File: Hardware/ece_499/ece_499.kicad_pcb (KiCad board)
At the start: 2 copper layers, 100 x 70 mm, 44 parts, among them J1 Conn_01x04, J2 Conn_01x04, J3 Conn_01x04, J4 Conn_01x04, J5 Conn_01x04, Q1 DMN2004WK, Q2 DMN2004WK, Q3 DMN2004WK, Q4 DMN2004WK, SW1 RotaryEncoder_Switch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

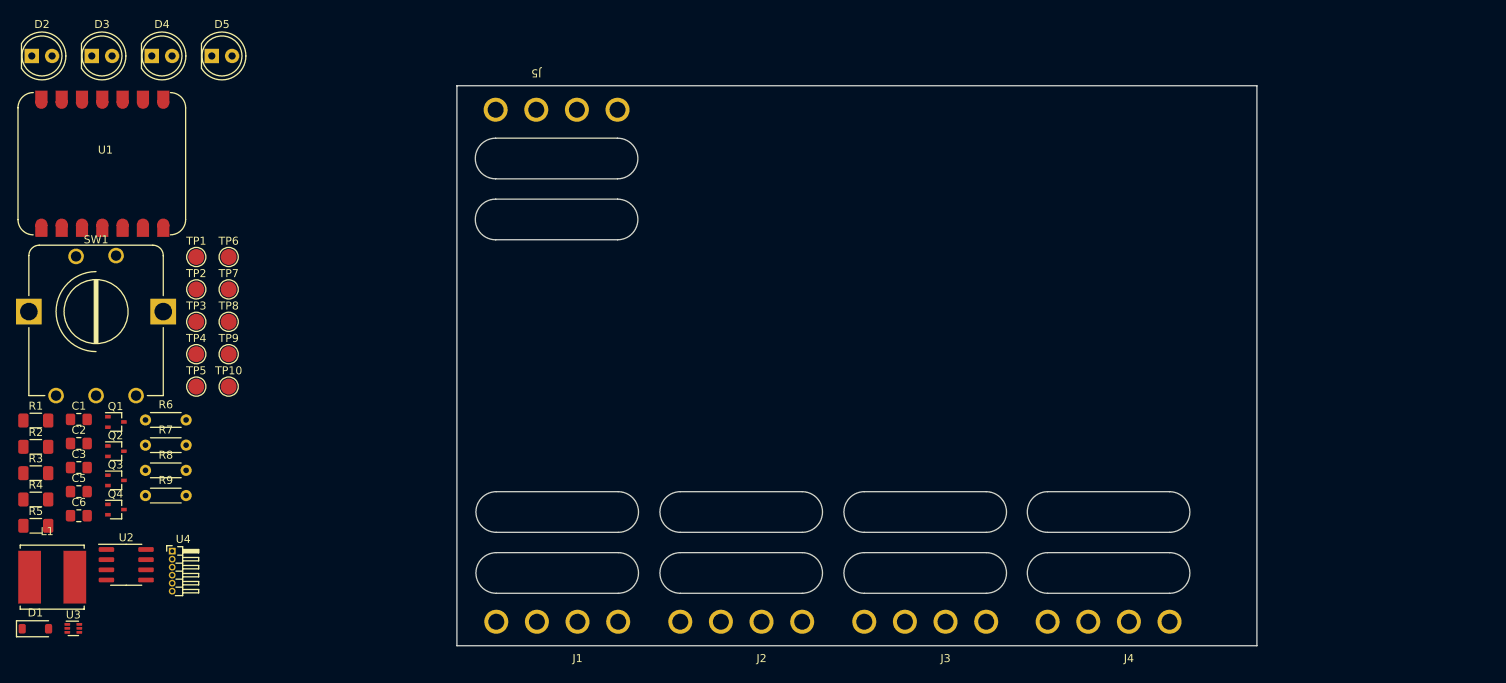
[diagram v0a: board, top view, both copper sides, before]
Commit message: Initial PCB layout and fix reg schema
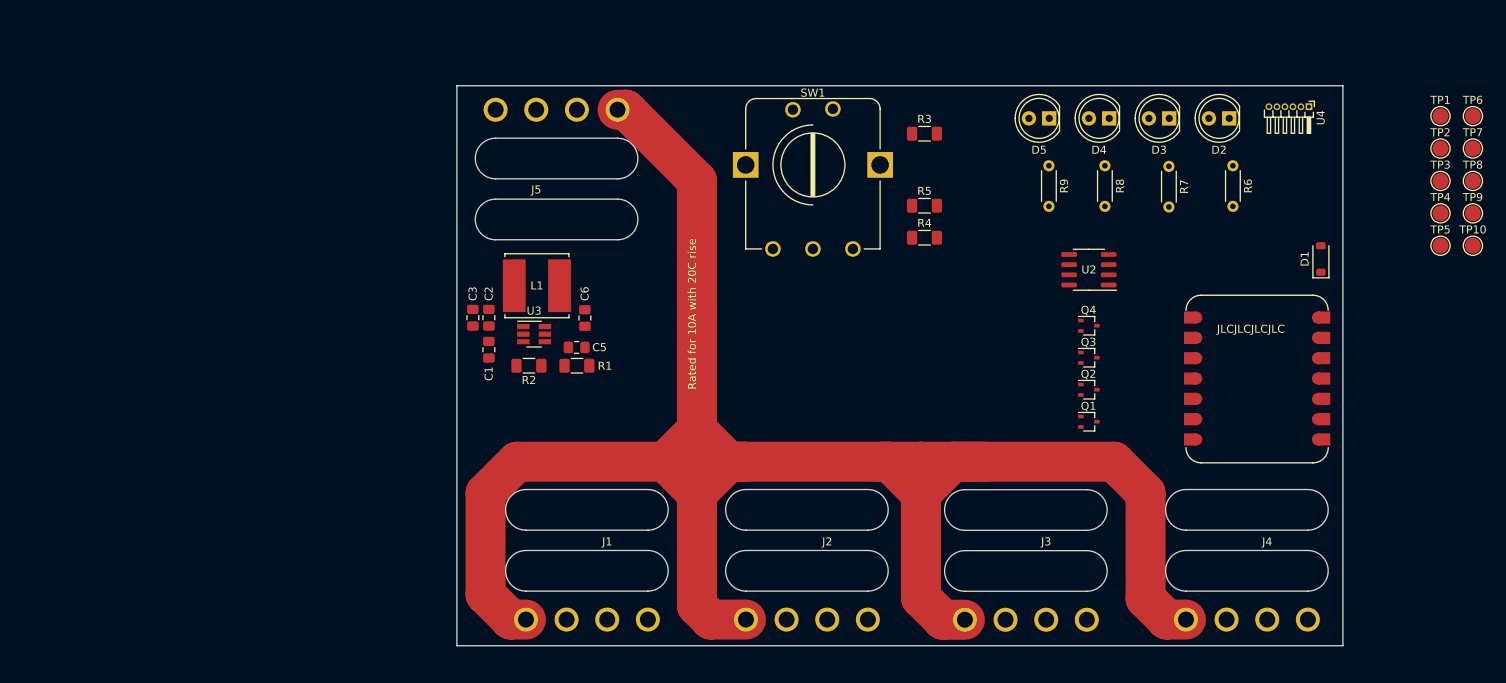
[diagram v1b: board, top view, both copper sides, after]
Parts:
- U3: footprint Package_TO_SOT_SMD:SOT-563 -> Package_TO_SOT_SMD:SOT-23-6_Handsoldering
- moved D1 167.2 mm to (208.0, 51.6), turned to 90 degrees
- moved TP1 156.5 mm to (222.9, 33.8)
- moved TP10 156.5 mm to (227.0, 50.0)
- moved TP2 156.5 mm to (222.9, 37.9)
- moved TP3 156.5 mm to (222.9, 41.9)
- moved TP4 156.5 mm to (222.9, 46.0)
- moved TP5 156.5 mm to (222.9, 50.0)
- moved TP6 156.5 mm to (227.0, 33.8)
- moved TP7 156.5 mm to (227.0, 37.9)
- moved TP8 156.5 mm to (227.0, 41.9)
- moved TP9 156.5 mm to (227.0, 46.0)
- moved U1 153.2 mm to (191.1, 77.1), turned to 90 degrees
- moved U4 152.6 mm to (206.5, 32.6), turned to -90 degrees
- moved D2 149.9 mm to (196.5, 34.1), turned to 180 degrees
- moved R6 139.6 mm to (197.0, 40.0), turned to -90 degrees
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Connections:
- U3 pad 1: +12V -> GND
- U3 pad 3: GND -> +12V
- U3 pad 4: Net-(U3-BST) -> Net-(U3-FB)
- U3 pad 6: Net-(U3-FB) -> Net-(U3-BST)
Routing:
- net +12V: track 0.00 -> 262.2 mm
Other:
- board size 100 x 70 mm -> 110.8 x 70 mm
- board text added: "JLCJLCJLCJLC"
- board text added: "Rated for 10A with 20C rise"

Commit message: Add new encoder design to initial PCB layout
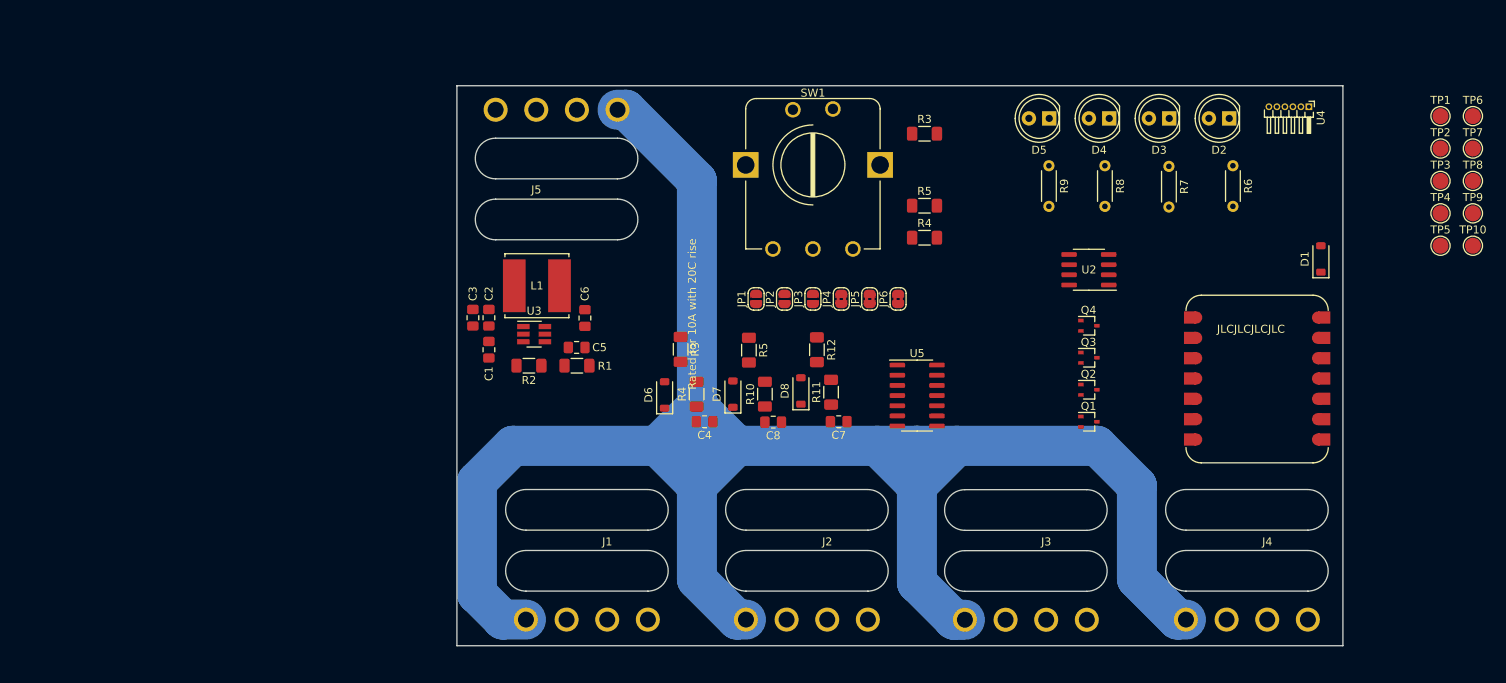
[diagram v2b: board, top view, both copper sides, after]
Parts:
- added C4: 22u, Capacitor_SMD:C_0805_2012Metric_Pad1.18x1.45mm_HandSolder, F.Cu at (131.0, 72.0)
- added C7: 22u, Capacitor_SMD:C_0805_2012Metric_Pad1.18x1.45mm_HandSolder, F.Cu at (147.7, 72.0)
- added C8: 22u, Capacitor_SMD:C_0805_2012Metric_Pad1.18x1.45mm_HandSolder, F.Cu at (139.5, 72.0)
- added D6: B5817W, Diode_SMD:D_SOD-123, F.Cu at (126.0, 68.7)
- added D7: B5817W, Diode_SMD:D_SOD-123, F.Cu at (134.5, 68.5)
- added D8: B5817W, Diode_SMD:D_SOD-123, F.Cu at (143.0, 68.2)
- added JP1: SolderJumper_2_Open, Jumper:SolderJumper-2_P1.3mm_Open_RoundedPad1.0x1.5mm, F.Cu at (137.4, 56.6)
- added JP2: SolderJumper_2_Open, Jumper:SolderJumper-2_P1.3mm_Open_RoundedPad1.0x1.5mm, F.Cu at (140.9, 56.6)
- added JP3: SolderJumper_2_Open, Jumper:SolderJumper-2_P1.3mm_Open_RoundedPad1.0x1.5mm, F.Cu at (144.5, 56.6)
- added JP4: SolderJumper_2_Bridged, Jumper:SolderJumper-2_P1.3mm_Bridged2Bar_RoundedPad1.0x1.5mm, F.Cu at (148.1, 56.6)
- added JP5: SolderJumper_2_Bridged, Jumper:SolderJumper-2_P1.3mm_Bridged2Bar_RoundedPad1.0x1.5mm, F.Cu at (151.6, 56.6)
- added JP6: SolderJumper_2_Bridged, Jumper:SolderJumper-2_P1.3mm_Bridged2Bar_RoundedPad1.0x1.5mm, F.Cu at (155.2, 56.6)
- added R10: 3.3k, Resistor_SMD:R_1206_3216Metric_Pad1.30x1.75mm_HandSolder, F.Cu at (138.5, 68.5)
- added R11: 2.7k, Resistor_SMD:R_1206_3216Metric_Pad1.30x1.75mm_HandSolder, F.Cu at (146.8, 68.3)
- added R12: 3.3k, Resistor_SMD:R_1206_3216Metric_Pad1.30x1.75mm_HandSolder, F.Cu at (145.0, 63.0)
- added R3: 2.7k, Resistor_SMD:R_1206_3216Metric_Pad1.30x1.75mm_HandSolder, F.Cu at (128.0, 63.0)
- added R4: 3.3k, Resistor_SMD:R_1206_3216Metric_Pad1.30x1.75mm_HandSolder, F.Cu at (130.0, 68.5)
- added R5: 2.7k, Resistor_SMD:R_1206_3216Metric_Pad1.30x1.75mm_HandSolder, F.Cu at (136.5, 63.0)
- added U5: CD74HC14M96, Package_SO:SO-14_3.9x8.65mm_P1.27mm, F.Cu at (157.5, 68.7)
- SW1: value RotaryEncoder_Switch -> Encoder
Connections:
- SW1 pad A: Net-(R5-Pad1) -> encoder_A
- SW1 pad B: Net-(R4-Pad1) -> encoder_B
- SW1 pad S1: Net-(R3-Pad1) -> encoder_sw
- SW1 pad S2: Net-(U1-D8) -> GND
- U1 pad 13: Net-(U1-D8) -> controller_sw
- U1 pad 14: Net-(U1-RX_D7) -> controller_B
- U1 pad 7: Net-(U1-TX_D6) -> controller_A
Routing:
- net +12V: track 262.2 -> 266.9 mm

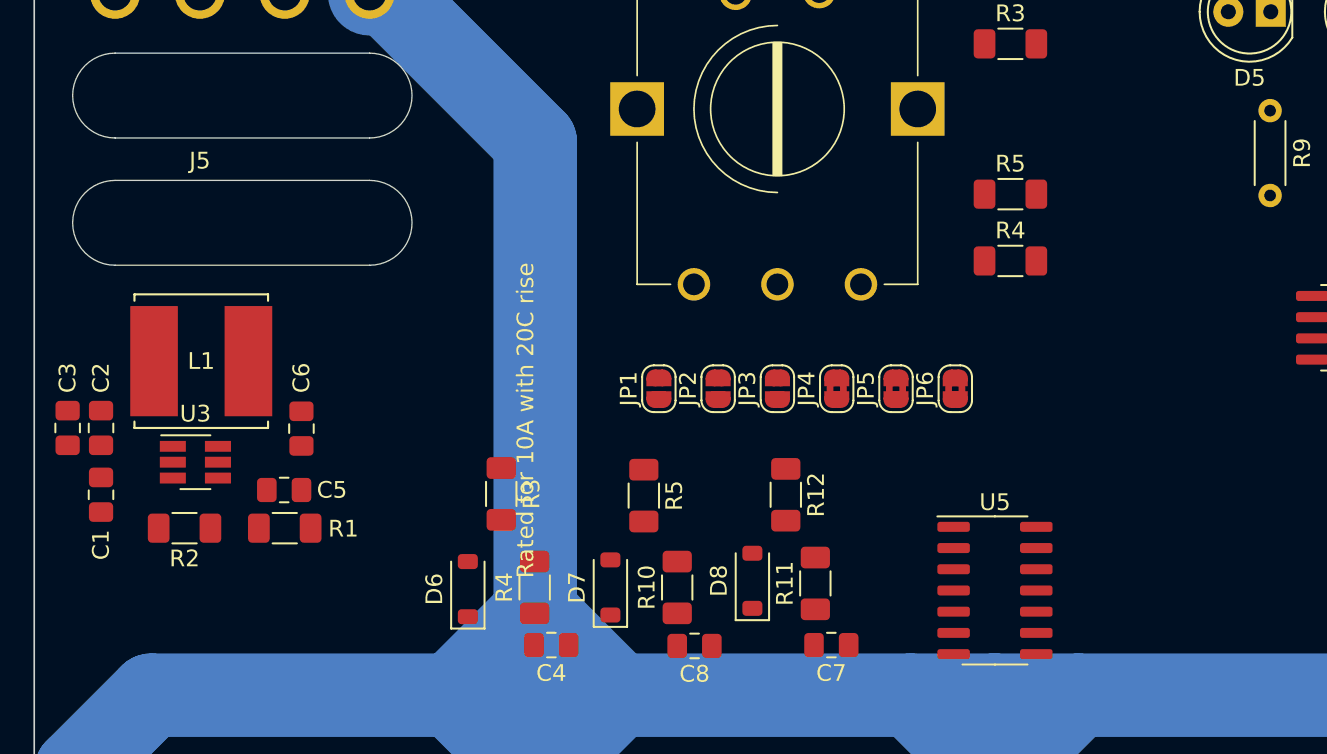
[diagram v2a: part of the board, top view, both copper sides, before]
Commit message: 5v reg circuit on PCB
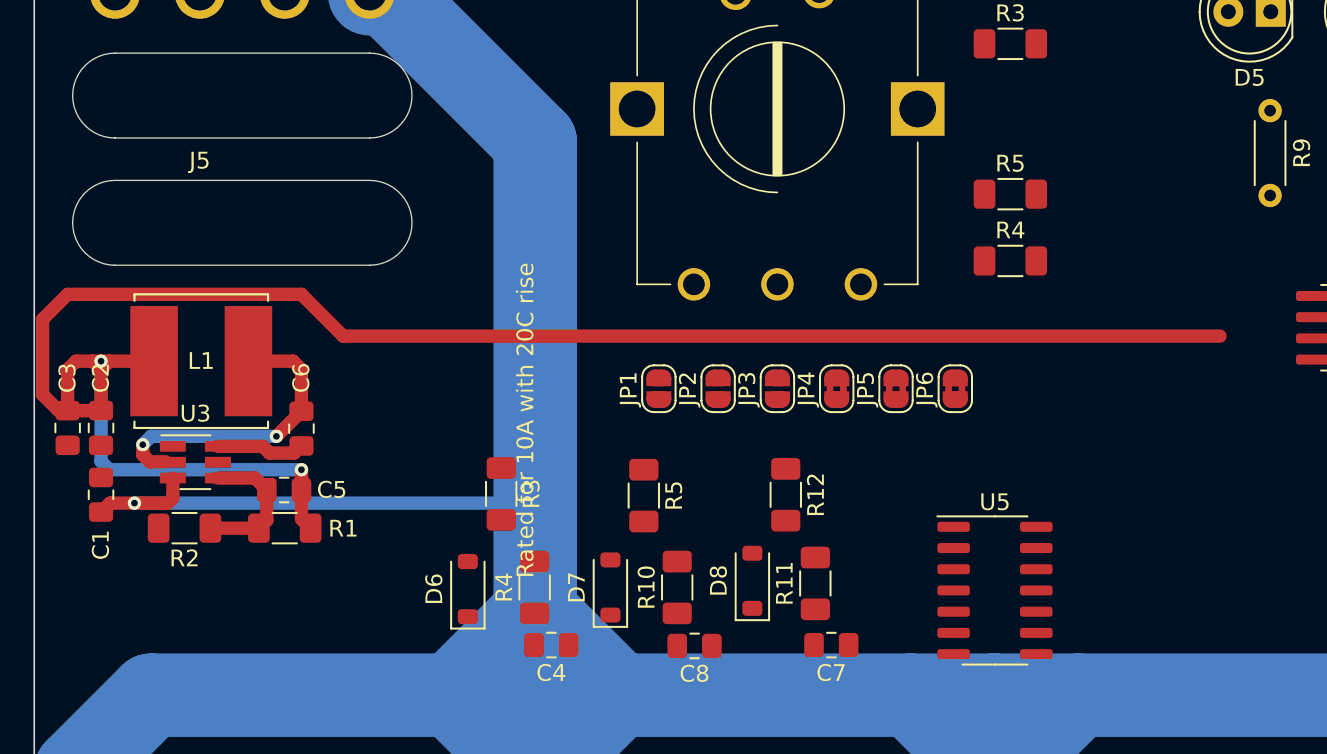
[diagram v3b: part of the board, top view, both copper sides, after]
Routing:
- net +5V: track 0.00 -> 114.7 mm, vias 0 -> 2
- net +12V: track 266.9 -> 296.7 mm, vias 0 -> 1
- net Net-(U3-SW): track 0.00 -> 18.4 mm, vias 0 -> 2
- net Net-(U3-FB): track 0.00 -> 8.61 mm
- net Net-(U3-BST): track 0.00 -> 5.34 mm
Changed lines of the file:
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@@
     (effects (font (size 1 1) (thickness 0.15)) (justify left bottom))
   )
+  (segment (start 104.5375 63.5) (end 104 64.0375) (width 0.8) (layer "F.Cu") (net 1))
+  (segment (start 108.3 62) (end 108.3 63.2) (width 0.8) (layer "F.Cu") (net 1))
+  (segment (start 108 63.5) (end 104.5375 63.5) (width 0.8) (layer "F.Cu") (net 1))
+  (segment (start 108.3 63.2) (end 108 63.5) (width 0.8) (layer "F.Cu") (net 1))
+  (via (at 106 63.5) (size 0.8) (drill 0.4) (layers "F.Cu" "B.Cu") (net 1))
   (segment (start 162.122801 96.75) (end 157.5 92.127199) (width 5) (layer "B.Cu") (net 1))
   (segment (start 121.125738 33) (end 130 41.874262) (width 5) (layer "B.Cu") (net 1))
@@
   (segment (start 130 70) (end 135 75) (width 5) (layer "B.Cu") (net 1))
   (segment (start 130 80) (end 125 75) (width 5) (layer "B.Cu") (net 1))
+  (segment (start 130 41.874262) (end 130 63.5) (width 5) (layer "B.Cu") (net 1))
   (segment (start 130 91.711037) (end 130 80) (width 5) (layer "B.Cu") (net 1))
   (segment (start 135.018463 96.7295) (end 130 91.711037) (width 5) (layer "B.Cu") (net 1))
   (segment (start 157.5 80) (end 152.5 75) (width 5) (layer "B.Cu") (net 1))
   (segment (start 107 75) (end 125 75) (width 5) (layer "B.Cu") (net 1))
+  (segment (start 130 63.5) (end 130 70) (width 5) (layer "B.Cu") (net 1))
   (segment (start 120.08 33) (end 121.125738 33) (width 5) (layer "B.Cu") (net 1))
   (segment (start 108.63 96.7295) (end 105.7295 96.7295) (width 5) (layer "B.Cu") (net 1))
@@
   (segment (start 135 75) (end 157.5 75) (width 5) (layer "B.Cu") (net 1))
   (segment (start 125 75) (end 130 70) (width 5) (layer "B.Cu") (net 1))
+  (segment (start 106 63.5) (end 130 63.5) (width 0.8) (layer "B.Cu") (net 1))
   (segment (start 102.5 79.5) (end 107 75) (width 5) (layer "B.Cu") (net 1))
   (segment (start 157.5 75) (end 180 75) (width 5) (layer "B.Cu") (net 1))
   (segment (start 162.5 75) (end 157.5 80) (width 5) (layer "B.Cu") (net 1))
-  (segment (start 130 41.874262) (end 130 70) (width 5) (layer "B.Cu") (net 1))
   (segment (start 163.5 96.75) (end 162.122801 96.75) (width 5) (layer "B.Cu") (net 1))
   (segment (start 185 80) (end 180 75) (width 5) (layer "B.Cu") (net 1))
   (segment (start 190.084262 96.7295) (end 191.13 96.7295) (width 5) (layer "B.Cu") (net 1))
+  (segment (start 101.4625 57.9625) (end 100.5 57) (width 0.8) (layer "F.Cu") (net 3))
+  (segment (start 104.5 55) (end 104 55) (width 0.8) (layer "F.Cu") (net 3))
+  (segment (start 103.5 55) (end 102.5 55) (width 0.8) (layer "F.Cu") (net 3))
+  (segment (start 116.003012 64.453012) (end 116.55 65) (width 0.8) (layer "F.Cu") (net 3))
+  (segment (start 107.175 55) (end 104.5 55) (width 0.8) (layer "F.Cu") (net 3))
+  (segment (start 118.5 53.5) (end 171 53.5) (width 0.8) (layer "F.Cu") (net 3))
+  (segment (start 102 51) (end 116 51) (width 0.8) (layer "F.Cu") (net 3))
+  (segment (start 100.5 57) (end 100.5 52.5) (width 0.8) (layer "F.Cu") (net 3))
+  (segment (start 102 55.5) (end 102 57.9625) (width 0.8) (layer "F.Cu") (net 3))
+  (segment (start 102 57.9625) (end 101.4625 57.9625) (width 0.8) (layer "F.Cu") (net 3))
+  (segment (start 104 55.5) (end 103.5 55) (width 0.8) (layer "F.Cu") (net 3))
+  (segment (start 116.003012 62.714131) (end 116.003012 61.503012) (width 0.8) (layer "F.Cu") (net 3))
+  (segment (start 102.5 55) (end 102 55.5) (width 0.8) (layer "F.Cu") (net 3))
+  (segment (start 116 51) (end 118.5 53.5) (width 0.8) (layer "F.Cu") (net 3))
+  (segment (start 100.5 52.5) (end 102 51) (width 0.8) (layer "F.Cu") (net 3))
+  (segment (start 104.5 55) (end 104 55.5) (width 0.8) (layer "F.Cu") (net 3))
+  (segment (start 116.003012 61.503012) (end 116 61.5) (width 0.8) (layer "F.Cu") (net 3))
+  (segment (start 104 55.5) (end 104 55) (width 0.8) (layer "F.Cu") (net 3))
+  (segment (start 104 55) (end 103.5 55) (width 0.8) (layer "F.Cu") (net 3))
+  (segment (start 104 57.9625) (end 104 55.5) (width 0.8) (layer "F.Cu") (net 3))
+  (segment (start 116.003012 62.714131) (end 116.003012 64.453012) (width 0.8) (layer "F.Cu") (net 3))
+  (segment (start 104 57.9625) (end 102 57.9625) (width 0.8) (layer "F.Cu") (net 3))
+  (via (at 104 55) (size 0.8) (drill 0.4) (layers "F.Cu" "B.Cu") (net 3))
+  (via (at 116 61.5) (size 0.8) (drill 0.4) (layers "F.Cu" "B.Cu") (net 3))
+  (segment (start 104 61) (end 104 55) (width 0.8) (layer "B.Cu") (net 3))
+  (segment (start 116 61.5) (end 104.5 61.5) (width 0.8) (layer "B.Cu") (net 3))
+  (segment (start 104.5 61.5) (end 104 61) (width 0.8) (layer "B.Cu") (net 3))
+  (segment (start 113.45 65) (end 110.55 65) (width 0.8) (layer "F.Cu") (net 4))
+  (segment (start 111 62) (end 113.213881 62) (width 0.8) (layer "F.Cu") (net 4))
+  (segment (start 113.213881 62) (end 113.928012 62.714131) (width 0.8) (layer "F.Cu") (net 4))
+  (segment (start 113.928012 64.521988) (end 113.45 65) (width 0.8) (layer "F.Cu") (net 4))
+  (segment (start 113.928012 62.714131) (end 113.928012 64.521988) (width 0.8) (layer "F.Cu") (net 4))
+  (segment (start 106.5 60) (end 106.5 60.605) (width 0.8) (layer "F.Cu") (net 5))
+  (segment (start 116 55.5) (end 115.5 55) (width 0.8) (layer "F.Cu") (net 5))
+  (segment (start 106.5 60.605) (end 106.92 61.025) (width 0.8) (layer "F.Cu") (net 5))
+  (segment (start 116 58) (end 114.5 59.5) (width 0.8) (layer "F.Cu") (net 5))
+  (segment (start 115.5 55) (end 112.825 55) (width 0.8) (layer "F.Cu") (net 5))
+  (segment (start 116 58) (end 116 55.5) (width 0.8) (layer "F.Cu") (net 5))
+  (segment (start 106.92 61.025) (end 107.860786 61.025) (width 0.8) (layer "F.Cu") (net 5))
+  (via (at 114.5 59.5) (size 0.8) (drill 0.4) (layers "F.Cu" "B.Cu") (net 5))
+  (via (at 106.5 60) (size 0.8) (drill 0.4) (layers "F.Cu" "B.Cu") (net 5))
+  (segment (start 107 59.5) (end 106.5 60) (width 0.8) (layer "B.Cu") (net 5))
+  (segment (start 114.5 59.5) (end 107 59.5) (width 0.8) (layer "B.Cu") (net 5))
+  (segment (start 111 60.1) (end 113.685786 60.1) (width 0.8) (layer "F.Cu") (net 6))
+  (segment (start 114.085787 60.500001) (end 115.574999 60.500001) (width 0.8) (layer "F.Cu") (net 6))
+  (segment (start 115.574999 60.500001) (end 116 60.075) (width 0.8) (layer "F.Cu") (net 6))
+  (segment (start 113.685786 60.1) (end 114.085787 60.500001) (width 0.8) (layer "F.Cu") (net 6))
 )
